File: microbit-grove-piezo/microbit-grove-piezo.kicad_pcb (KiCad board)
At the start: 2 copper layers, 59 x 15.4 mm, 8 parts, among them J1 microbit_smd_socket, J2 GROVE-CONNECTOR-SMD_4+2P-2.0_, J3 GROVE-CONNECTOR-SMD_4+2P-2.0_, J4 GROVE-CONNECTOR-SMD_4+2P-2.0_, J5 GROVE-CONNECTOR-SMD_4+2P-2.0_

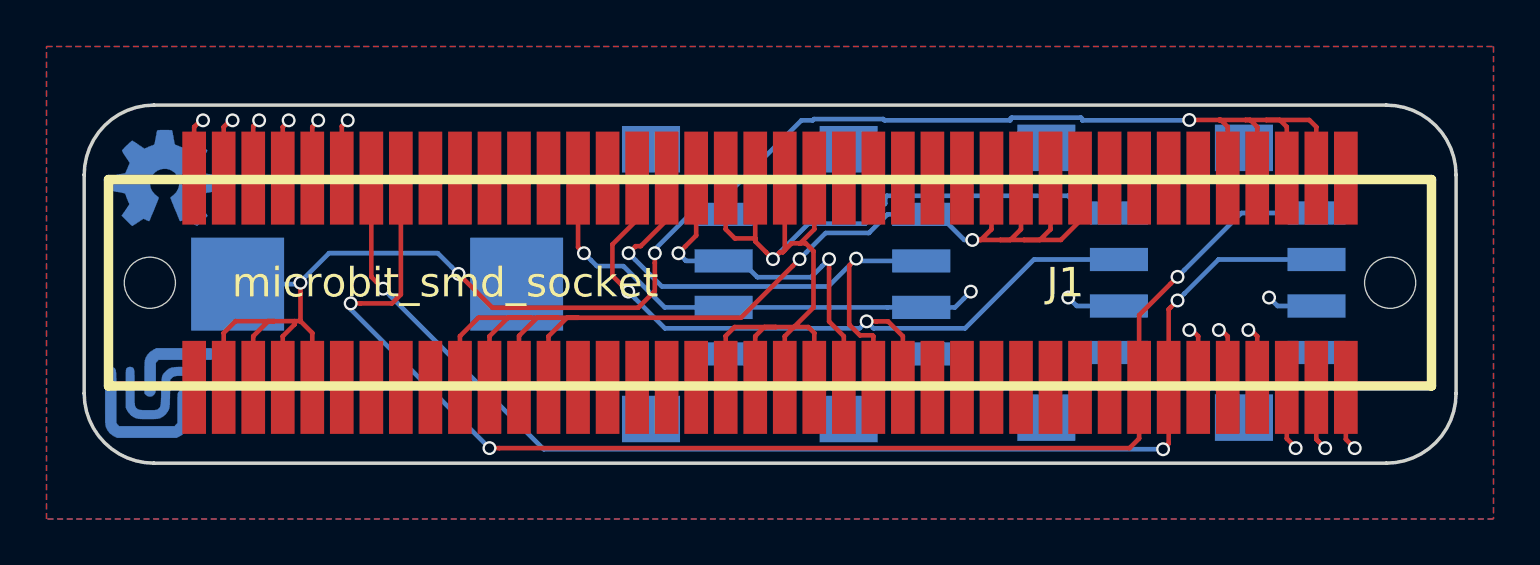
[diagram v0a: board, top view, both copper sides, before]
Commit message: Change pinout
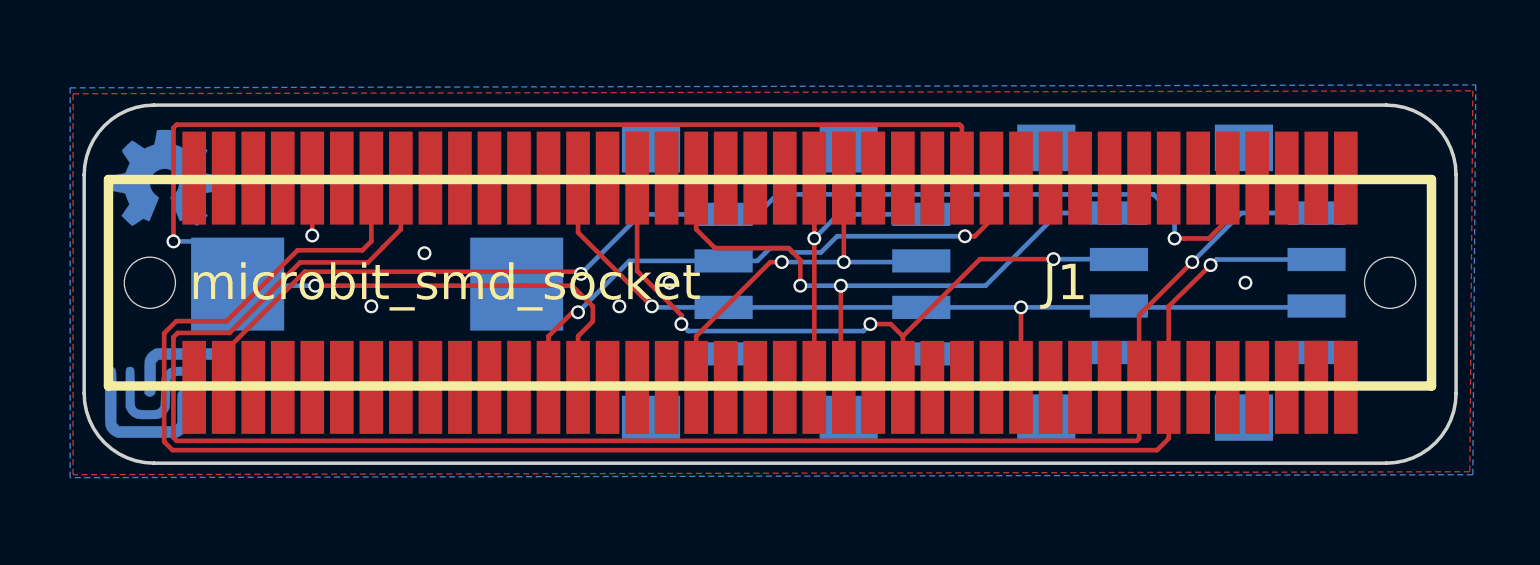
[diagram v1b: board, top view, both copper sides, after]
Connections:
- J1 pad 10: (no net) -> Net-(J1-Pad10)
- J1 pad 11: (no net) -> Net-(J1-Pad11)
- J1 pad 12: (no net) -> Net-(J1-Pad12)
- J1 pad 13: (no net) -> MB_12
- J1 pad 15: MB_14 -> Net-(J1-Pad15)
- J1 pad 17: (no net) -> Net-(J1-Pad17)
- J1 pad 29: (no net) -> Net-(J1-Pad29)
- J1 pad 30: (no net) -> Net-(J1-Pad30)
- J1 pad 31: (no net) -> Net-(J1-Pad31)
- J1 pad 32: (no net) -> Net-(J1-Pad32)
- J1 pad 33: (no net) -> Net-(J1-Pad33)
- J1 pad 34: (no net) -> MB_8
- J1 pad 35: (no net) -> Net-(J1-Pad35)
- J1 pad 36: (no net) -> Net-(J1-Pad36)
- J1 pad 37: (no net) -> Net-(J1-Pad37)
- J1 pad 38: (no net) -> MB_12
- J1 pad 4: (no net) -> Net-(J1-Pad4)
- J1 pad 40: MB_14 -> Net-(J1-Pad40)
- J1 pad 42: (no net) -> Net-(J1-Pad42)
- J1 pad 5: (no net) -> Net-(J1-Pad5)
- J1 pad 6: (no net) -> Net-(J1-Pad6)
- J1 pad 7: (no net) -> Net-(J1-Pad7)
- J1 pad 8: (no net) -> Net-(J1-Pad8)
- J1 pad 9: (no net) -> MB_8
- J2 pad 2: MB_13 -> MB_1
- J2 pad SS1: (no net) -> Net-(J2-PadSS1)
- J2 pad SS2: (no net) -> Net-(J2-PadSS2)
- J3 pad 1: MB_1 -> MB_2
- J3 pad 2: MB_14 -> MB_12
- J3 pad SS1: (no net) -> Net-(J3-PadSS1)
- J3 pad SS2: (no net) -> Net-(J3-PadSS2)
- J4 pad 1: MB_2 -> MB_13
- J4 pad SS1: (no net) -> Net-(J4-PadSS1)
- J4 pad SS2: (no net) -> Net-(J4-PadSS2)
- J5 pad SS1: (no net) -> Net-(J5-PadSS1)
- J5 pad SS2: (no net) -> Net-(J5-PadSS2)
- LS1 pad 1: MB_0 -> MB_8
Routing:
- net MB_8: track 0.00 -> 64.1 mm, vias 0 -> 2
- net MB_GND: track 32.1 -> 2.47 mm, vias 12 -> 6
- net MB_2: track 50.6 -> 21.6 mm
- net MB_3V3: track 25.7 -> 51.6 mm, vias 4 -> 2
- net MB_14: track 24.2 -> 0.00 mm, vias 2 -> 0
- net MB_1: track 56.0 -> 32.9 mm
- net MB_0: track 80.8 -> 58.7 mm, vias 4 -> 2
- net MB_20: track 54.7 -> 76.2 mm, vias 3 -> 1
- net MB_12: track 0.00 -> 16.8 mm, vias 0 -> 2
- net MB_19: track 58.9 -> 74.6 mm, vias 3 -> 1
- net MB_13: track 16.5 -> 27.8 mm
- net MB_15: track 32.9 -> 29.9 mm, vias 2 -> 3
- added copper zone on F.Cu, net MB_GND
- removed copper zone on F.Cu, net MB_3V3
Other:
- board text added: "0 1 + -"
- board text added: "13 15 + -"
- board text added: "2 12 + -"
- board text removed: "0 13 + -"
- board text removed: "1 14 + -"
- board text removed: "2 15 + -"
